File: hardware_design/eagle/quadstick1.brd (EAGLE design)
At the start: 27 x 25.4 mm, 32 parts, among them J1 USB MICRO, U1 ATMEGA32U4-XUMU, Y1 16MHz KX-7

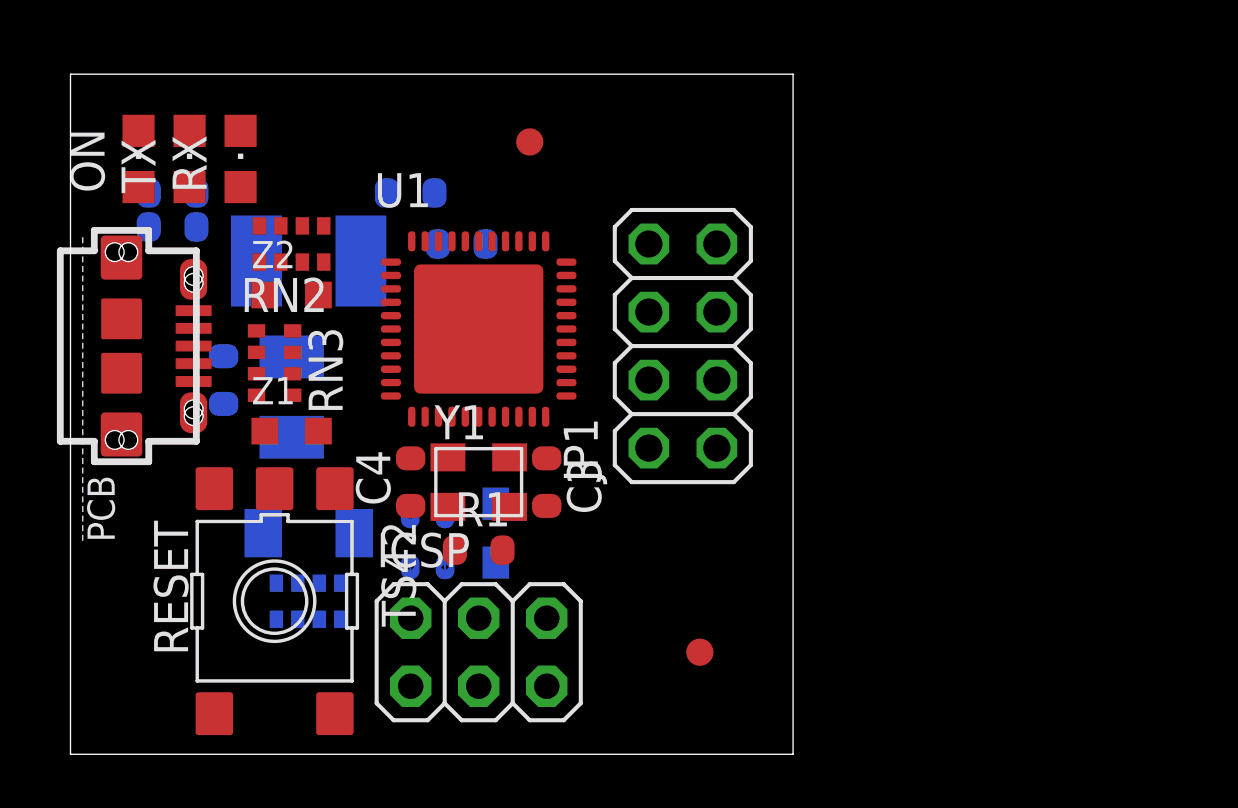
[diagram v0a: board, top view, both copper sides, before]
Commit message: Re-positioned all components for USB and Analog parts to top layer for easier reflow
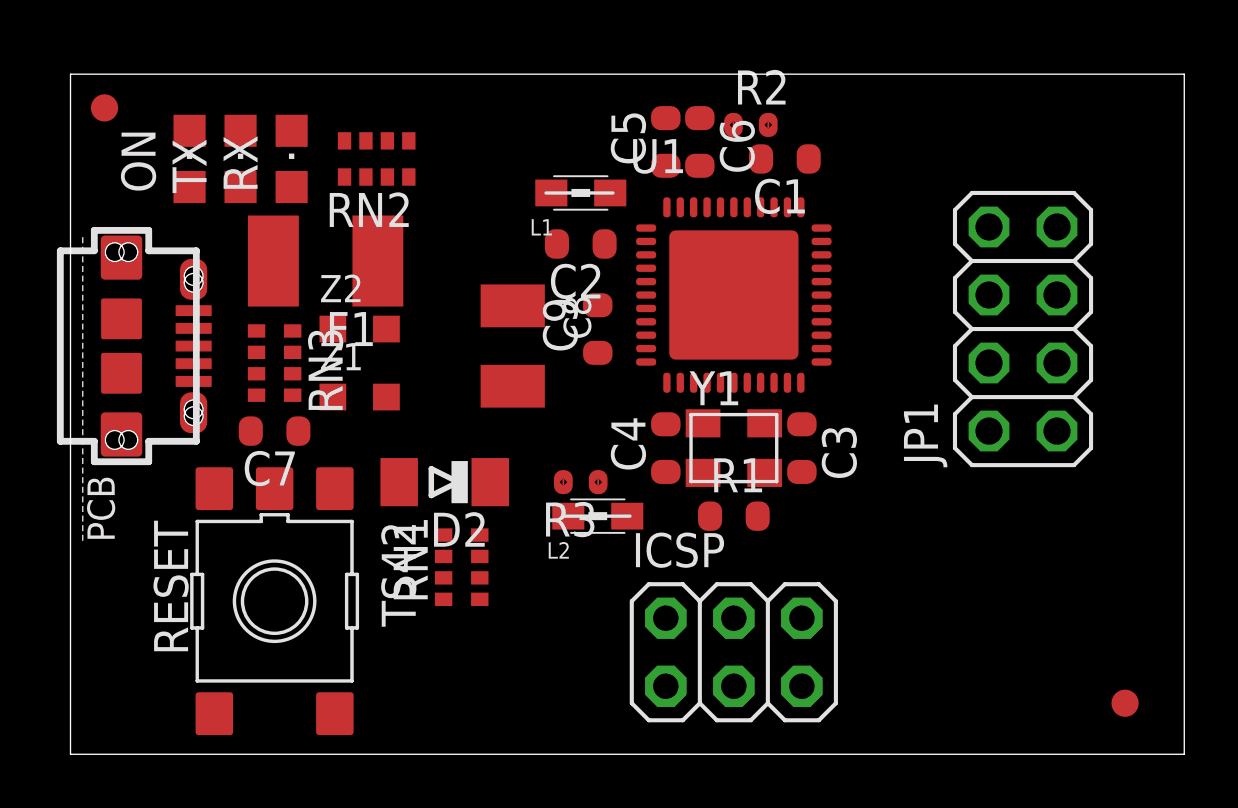
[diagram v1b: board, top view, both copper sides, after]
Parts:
- moved C1 22.9 mm to (26.7, 22.2), flipped to the top, turned to 180 degrees
- moved R2 18.9 mm to (25.4, 23.5), flipped to the top
- moved FID3 16.0 mm to (39.4, 1.91)
- moved FID2 15.9 mm to (1.27, 24.1)
- moved C2 15.3 mm to (19.1, 19.1), flipped to the top, turned to 180 degrees
- moved JP1 12.7 mm to (35.6, 15.9)
- moved C6 9.67 mm to (23.5, 22.9), flipped to the top, turned to 270 degrees
- moved C4 9.61 mm to (22.2, 11.4)
- moved R1 9.61 mm to (24.8, 8.89)
- moved U1 9.61 mm to (24.8, 17.1)
- moved Y1 9.61 mm to (24.8, 11.4)
- moved C3 9.61 mm to (27.3, 11.4)
- moved C5 9.53 mm to (22.2, 22.9), flipped to the top, turned to 90 degrees
- moved ICSP 9.53 mm to (24.8, 3.81)
- moved C9 8.64 mm to (19.7, 15.9), flipped to the top, turned to 90 degrees
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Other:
- board size 27 x 25.4 mm -> 41.6 x 25.4 mm
